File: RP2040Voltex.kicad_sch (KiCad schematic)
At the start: 70 parts, among them J2 SWD_Connector, SW1 SW_Push_Dual_x2, SW2 K2-1102SP-C4SC-04, U1 RT8096C, U2 W25Q128JVS, U3 RP2040, U4 PEC16-4015F-N0024, U5 PEC16-4015F-N0024, Y1 Crystal_GND24

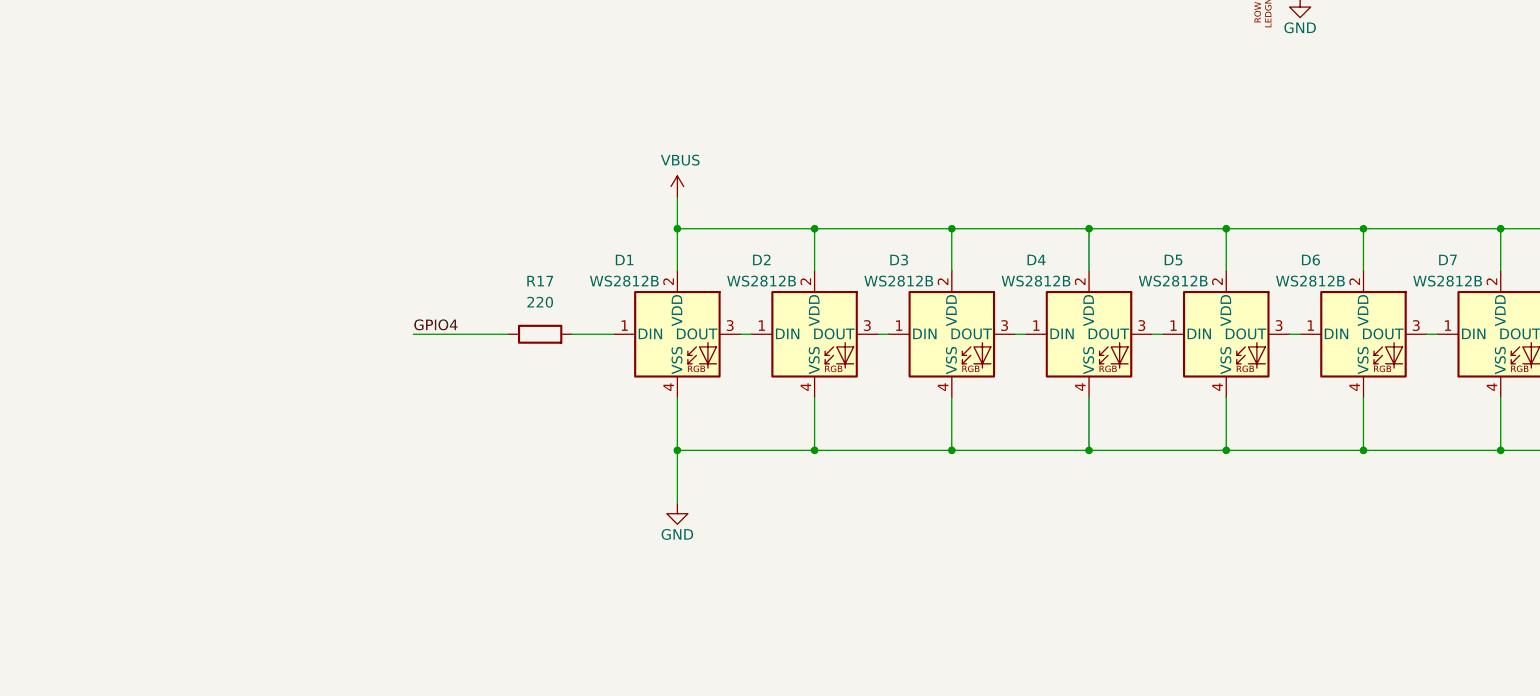
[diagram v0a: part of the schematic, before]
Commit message: Split led strips + Put usb boot underneath
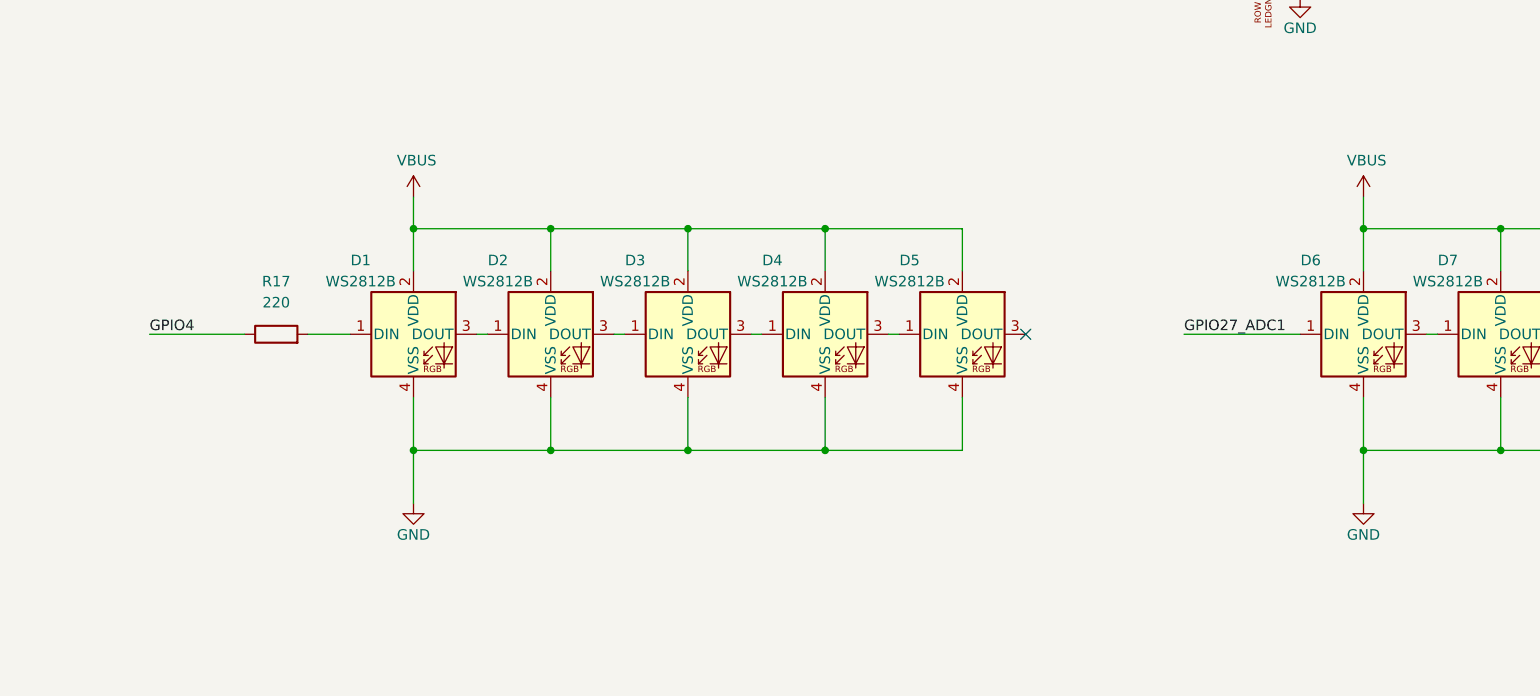
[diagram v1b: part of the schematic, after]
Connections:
- net GPIO27_ADC1: now also D6.1 (DIN)
- net at D5.3 (DOUT): no longer D6.1 (DIN)
- no-connect marks 3 -> 4
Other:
- moved on the sheet: D1, D2, D3, D4, D5, R17
